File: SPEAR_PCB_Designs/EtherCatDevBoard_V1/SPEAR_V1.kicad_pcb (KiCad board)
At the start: 4 copper layers, 44 x 55 mm, 112 parts, among them J1 USB_C_Receptacle_USB2.0_16P, J2 FTSH-107-01-F-DV-K-P-TR, J3 Conn_01x20_Pin, J4 Conn_01x20_Pin, J5 SM04B-GHS-TB, J6 SM04B-GHS-TB, SW1 SW_Push, T1 H1102NLT, T2 H1102NLT, U1 USBLC6-2SC6, U2 STM32F446RCT6, U3 AMS1117-3.3, U4 LAN9252I/ML, U5 24FC512-I/SN, U6 TPS2116DRL, Y1 16MHz, Y2 25MHz

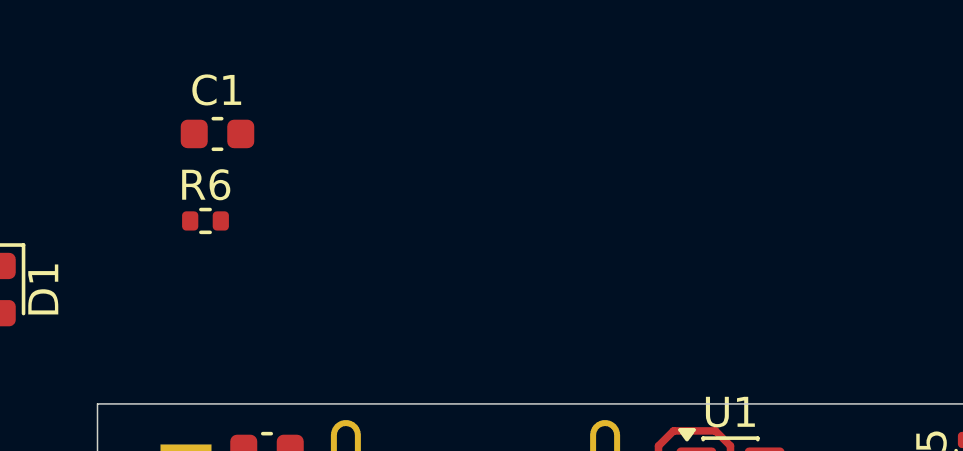
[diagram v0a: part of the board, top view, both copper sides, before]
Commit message: Finished etherCAT microcontroller dev board component selection. BOM is available. PCB layout incomplete.
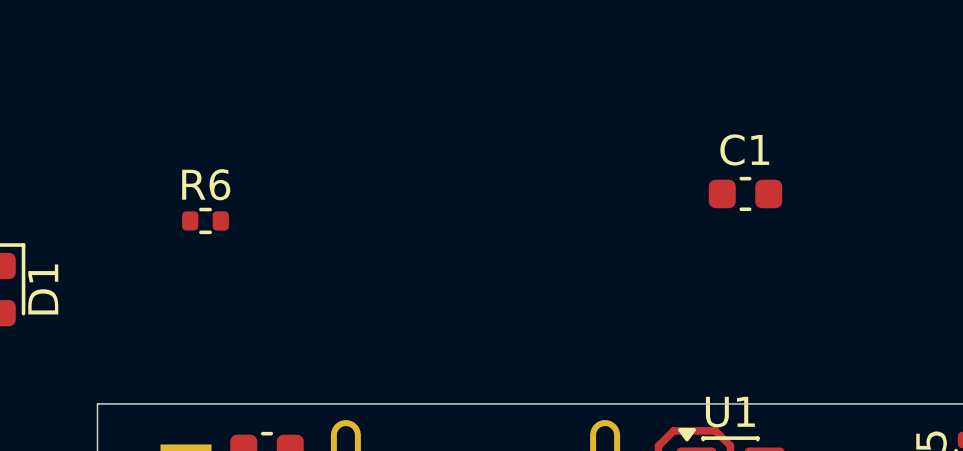
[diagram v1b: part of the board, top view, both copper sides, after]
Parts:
- moved C1 17.7 mm to (99.6, 95.0)
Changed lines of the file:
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@@
 	(footprint "Capacitor_SMD:C_0603_1608Metric"
 		(layer "F.Cu")
-		(at 82 93)
+		(at 99.6 95)
 		(descr "Capacitor SMD 0603 (1608 Metric), square (rectangular) end terminal, IPC-7351 nominal, (Body size source: IPC-SM-782 page 76, https://www.pcb-3d.com/wordpress/wp-content/uploads/ipc-sm-782a_amendment_1_and_2.pdf), generated with kicad-footprint-generator")
 		(tags "capacitor")

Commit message: Continued work on the Ethercat dev board. Unfinished.
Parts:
- added ?: , , F.Cu at (81.0, 155.0)
- added REF**: ToolingHole_1.152mm, MountingHole:ToolingHole_1.152mm, F.Cu at (119.0, 104.2)
- C1, C14, C52: value 10u -> 10uF
- C10, C2, C3, C4, C5, C6: value 100n -> 100nF
- C11, C12, C42, C43, C44, C45, C46, C47, C48, C49: value 10p -> 10pF
- C13: value 2.2u -> 2.2uF
- C15: value 22u -> 22uF
- C17, C19, C20, C21, C22, C23, C24, C25, C26, C27, C28, C29, C30, C35, C36: value 0.1uF -> 100nF
- C37, C40: value 1000 uF -> 1nF
- C38, C41: value 22n -> 22nF
- C39: value 0.1 uF -> 100nF
- C50, C51, C8, C9: value 1u -> 1uF
- C7: value 10n -> 10nF
- D1: value LED -> LED_RED
- D2: value LED -> LED_BLUE
- D3, D4: value LED -> LED_GREEN
- J1: footprint Connector_USB:USB_C_Receptacle_GCT_USB4105-xx-A_16P_TopMnt_Horizontal -> LAN9252 Footprints:USB_C_Receptacle_GCT_USB4105-xx-A_16P_TopMnt_Horizontal
- R10, R24, R6: value 1k -> 1kR
- R16, R18, R19: value 10k 1% -> 10kR 1%
- R2, R34: value 10k -> 10kR
- R21, R22: value 2k 0.1% -> 2kR 0.1%
- R3, R33, R4: value 5.1k -> 5.1kR
- R32: value 7.5k -> 7.5kR
- R8: value 12.1k 1% -> 12.1kR 1%
- U3: value AMS1117-3.3 -> AMS1117-3.3 SOT-223
- moved R2 38.8 mm to (93.8, 115.6), turned to 90 degrees
- moved C1 31.9 mm to (108.8, 125.6), turned to -90 degrees
- moved C23 31.6 mm to (97.8, 137.4), turned to -90 degrees
- moved C22 30.9 mm to (98.8, 137.4), turned to -90 degrees
- moved D1 30.2 mm to (104.5, 103.4), turned to 180 degrees
- moved C20 29.8 mm to (101.8, 137.4), turned to -90 degrees
- moved C21 29.8 mm to (100.8, 137.4), turned to -90 degrees
- moved R6 23.4 mm to (103.3, 104.7), turned to 180 degrees
- moved R32 20.4 mm to (87.6, 110.4), turned to -90 degrees
- moved C10 17.7 mm to (113.2, 110.7)
- moved C51 16.5 mm to (84.8, 107.0)
- moved R1 16.1 mm to (111.2, 110.7), turned to 0 degrees
- moved R33 15.6 mm to (89.1, 110.9)
- moved R34 13.4 mm to (83.1, 107.0), turned to 90 degrees
- moved C50 12.1 mm to (86.1, 110.9), turned to 0 degrees
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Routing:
- net /STM32F446RC/PC0: track 0.00 -> 50.1 mm, vias 0 -> 1
- net /STM32F446RC/PC1: track 0.00 -> 49.8 mm, vias 0 -> 1
- net /STM32F446RC/PC2: track 0.00 -> 49.7 mm, vias 0 -> 1
- net /STM32F446RC/PC3: track 0.00 -> 48.8 mm, vias 0 -> 1
- net /STM32F446RC/PA0: track 0.00 -> 45.8 mm, vias 0 -> 1
- net /STM32F446RC/PA1: track 0.00 -> 43.5 mm, vias 0 -> 1
- net /STM32F446RC/PA4: track 0.00 -> 37.9 mm, vias 0 -> 1
- net /STM32F446RC/PB2: track 0.00 -> 31.0 mm, vias 0 -> 1
- net /STM32F446RC/PB1: track 0.00 -> 30.6 mm, vias 0 -> 1
- net /STM32F446RC/PC5: track 0.00 -> 30.4 mm, vias 0 -> 1
- net /STM32F446RC/PB0: track 1.82 -> 31.2 mm
- net /STM32F446RC/SWO: track 0.00 -> 29.1 mm, vias 0 -> 2
- net /STM32F446RC/PB10: track 0.00 -> 28.7 mm, vias 0 -> 1
- net /STM32F446RC/NRST: track 0.00 -> 27.1 mm, vias 0 -> 2
- net /STM32F446RC/PB15: track 0.00 -> 26.3 mm, vias 0 -> 1
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- added copper zone on In2.Cu, net +5V
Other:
- outline, holes or cut-outs redrawn

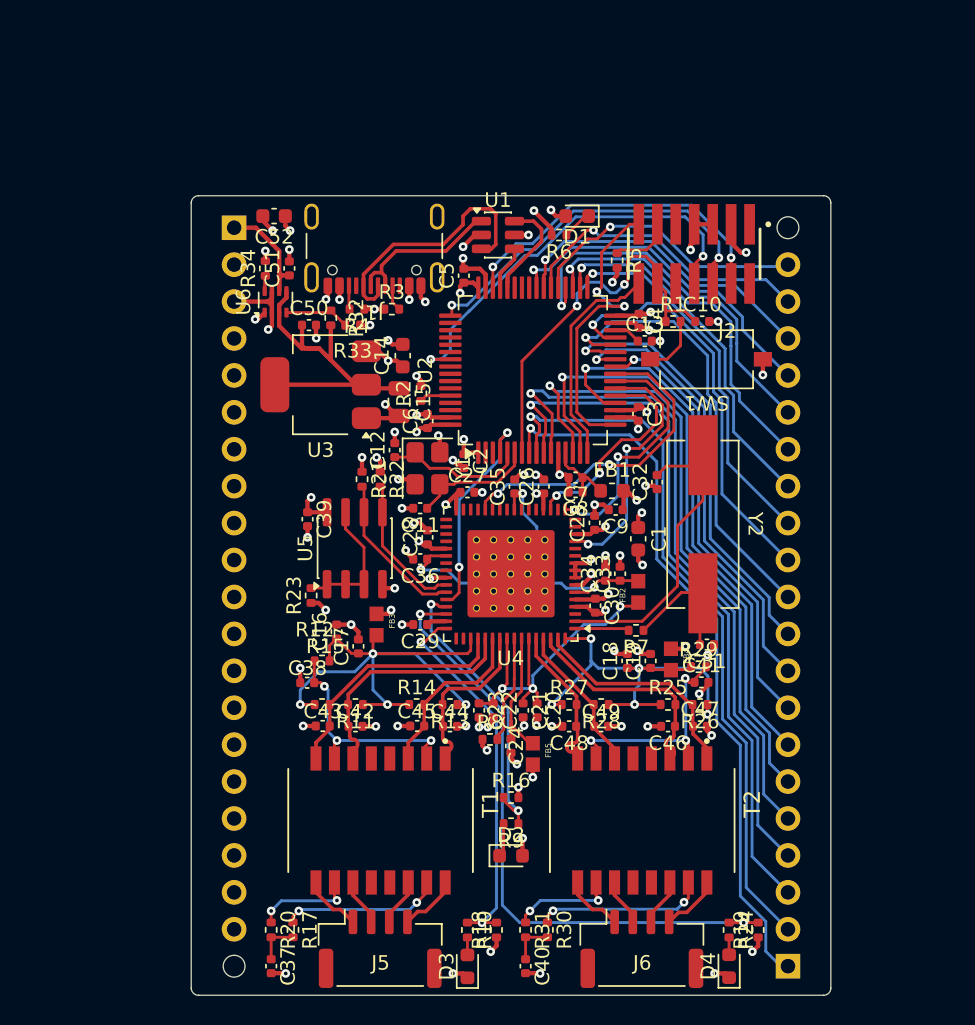
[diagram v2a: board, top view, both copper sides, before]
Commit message: Finished version 1.0 of the EtherCAT STM32 Development Board. Gerber files (and drill files) are available.
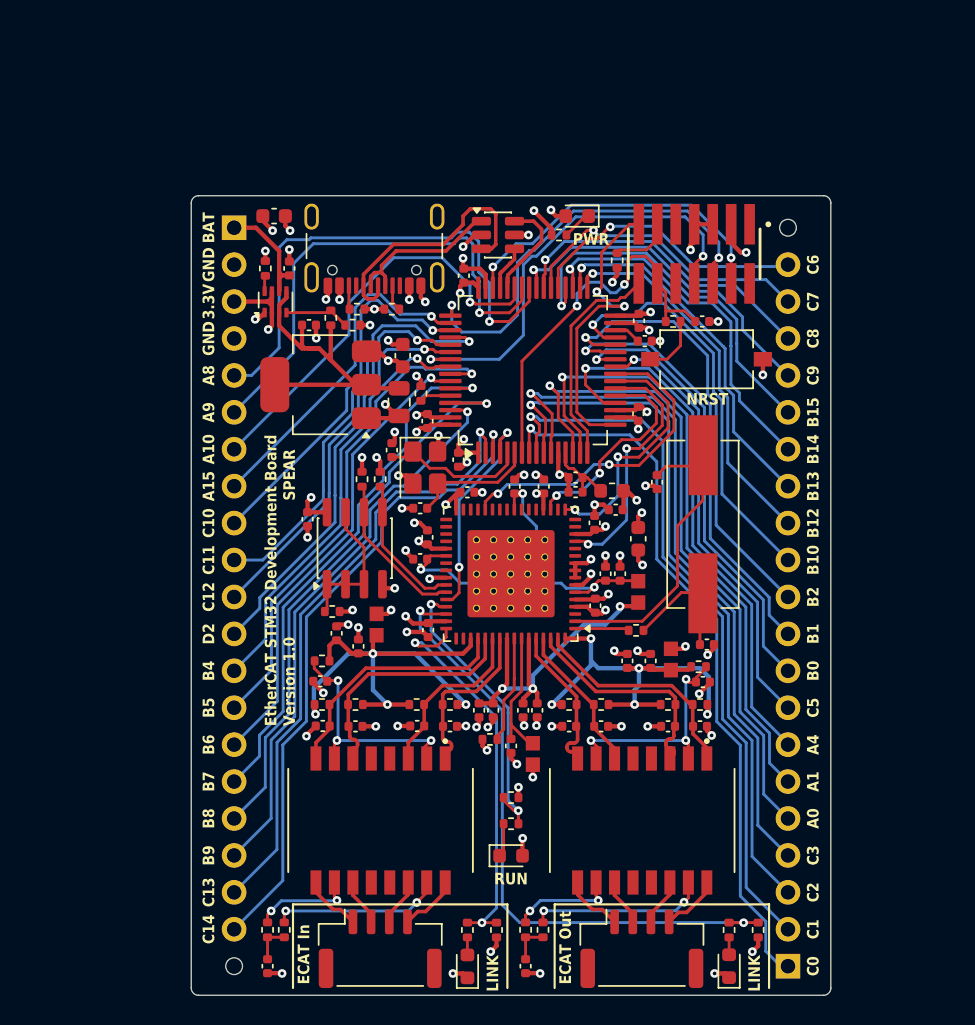
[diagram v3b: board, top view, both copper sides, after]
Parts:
- removed ?: , 
- added G***: LOGO, SPEAR Logos:spear_logo_10.0x10, B.Cu at (109.2, 145.0)
- added G***: LOGO, SPEAR Images:Blissey_Gun, B.Cu at (91.0, 145.0)
- added REF**: ToolingHole_1.152mm, MountingHole:ToolingHole_1.152mm, F.Cu at (81.0, 155.0)
- moved R23 1.82 mm to (87.7, 130.6), turned to 180 degrees
- moved C38 0.90 mm to (86.9, 135.4)
- moved C29 0.67 mm to (94.3, 131.9), turned to -90 degrees
- moved R17 0.60 mm to (84.4, 152.5)
- moved C2 0.38 mm to (96.4, 120.2)
- moved R30 0.30 mm to (102.2, 152.5)
- moved C37 0.25 mm to (83.2, 155.0)
- moved R20 0.25 mm to (83.2, 152.5)
- moved C12 0.20 mm to (91.8, 119.5)
- moved Y1 0.16 mm to (94.1, 120.7)
- moved C16 0.12 mm to (88.0, 132.1)
- moved C41 0.10 mm to (113.2, 135.4)
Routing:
- net /STM32F446RC/PC14: track 0.00 -> 44.8 mm, vias 0 -> 1
- net /STM32F446RC/PC13: track 0.00 -> 42.4 mm, vias 0 -> 1
- net /STM32F446RC/PB8: track 0.00 -> 39.5 mm, vias 0 -> 1
- net /STM32F446RC/PB9: track 0.00 -> 38.8 mm, vias 0 -> 1
- net /STM32F446RC/PB7: track 0.00 -> 37.1 mm, vias 0 -> 1
- net /STM32F446RC/PA8: track 0.00 -> 35.3 mm, vias 0 -> 1
- net /STM32F446RC/PB5: track 0.00 -> 34.3 mm, vias 0 -> 1
- net /STM32F446RC/PA9: track 0.00 -> 34.3 mm, vias 0 -> 1
- net /STM32F446RC/PB6: track 0.00 -> 32.3 mm, vias 0 -> 1
- net /STM32F446RC/PB4: track 0.00 -> 29.6 mm, vias 0 -> 1
- net /STM32F446RC/PC11: track 0.00 -> 29.3 mm, vias 0 -> 1
- net /STM32F446RC/PA10: track 0.00 -> 29.0 mm, vias 0 -> 1
- net /STM32F446RC/PD2: track 0.00 -> 28.4 mm, vias 0 -> 1
- net /STM32F446RC/PC12: track 0.00 -> 27.4 mm, vias 0 -> 1
- net /STM32F446RC/PC10: track 0.00 -> 25.5 mm, vias 0 -> 1
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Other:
- rule pad_to_mask_clearance: 0.1 -> 0
- board text added: "3.3V"
- board text added: "A0"
- board text added: "A1"
- board text added: "A10"
- board text added: "A15"
- board text added: "A4"
- board text added: "A8"
- board text added: "A9"
- board text added: "B0"
- board text added: "B1"
- board text added: "B10"
- board text added: "B12"
- board text added: "B13"
- board text added: "B14"
- board text added: "B15"
- board text added: "B2"
- board text added: "B4"
- board text added: "B5"
- board text added: "B6"
- board text added: "B7"
- board text added: "B8"
- board text added: "B9"
- board text added: "BAT"
- board text added: "C0"
- board text added: "C1"
- board text added: "C10"
- board text added: "C11"
- board text added: "C12"
- board text added: "C13"
- board text added: "C14"
- board text added: "C2"
- board text added: "C3"
- board text added: "C5"
- board text added: "C6"
- board text added: "C7"
- board text added: "C8"
- board text added: "C9"
- board text added: "D2"
- board text added: "ECAT In"
- board text added: "ECAT Out"
- board text added: "EtherCAT STM32 Development Board"
- board text added: "GND"
- board text added: "Henry Diep Chris Rivington Ronak Grover"
- board text added: "LINK"
- board text added: "NRST"
- board text added: "PWR"
- board text added: "RUN"
- board text added: "SPEAR"
- board text added: "Space Exploration Alberta Robotics 2026"
- board text added: "Version 1.0"
